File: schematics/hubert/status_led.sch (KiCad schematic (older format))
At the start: 8 parts, among them U8 ULN2003A

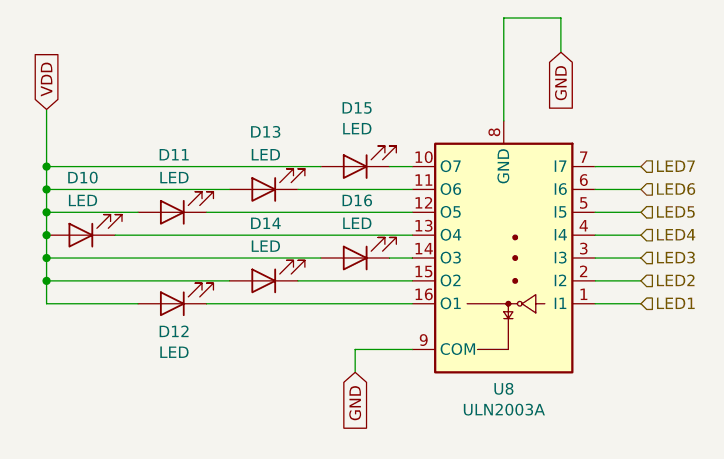
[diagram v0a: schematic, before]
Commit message: fixed ERC problems and added connector for input pins
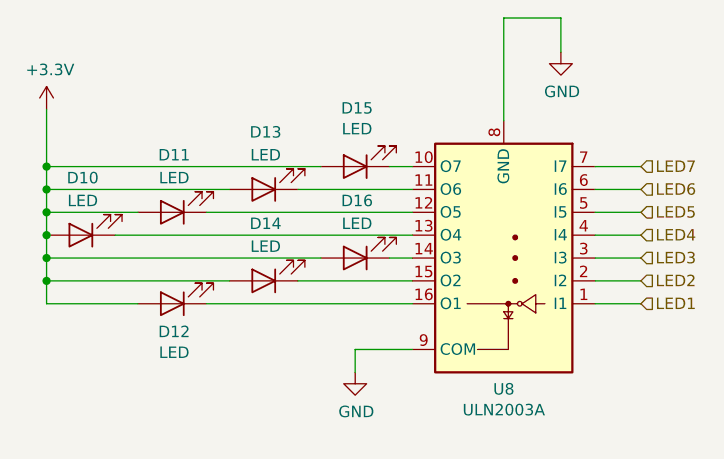
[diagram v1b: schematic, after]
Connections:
- net VDD renamed +3V3
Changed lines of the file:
@@
 Text HLabel 6850 3500 2    50   Input ~ 0
 LED7
-Text GLabel 5600 4400 3    50   Input ~ 0
-GND
 $Comp
 L Transistor_Array:ULN2003A U8
@@
 Wire Wire Line
 	5600 4300 5600 4400
-Text GLabel 6500 3000 3    50   Input ~ 0
-GND
 Wire Wire Line
 	6250 3300 6250 2850
@@
 Wire Wire Line
 	5450 3500 4250 3500
-Text GLabel 4250 3250 1    50   Input ~ 0
-VDD
 Wire Wire Line
 	4250 3250 4250 3500
@@
 Wire Wire Line
 	4250 4000 4250 4100
+$Comp
+L power:+3.3V #PWR0127
+U 1 1 5BE2D2EF
+P 4250 3250
+F 0 "#PWR0127" H 4250 3100 50  0001 C CNN
+F 1 "+3.3V" H 4265 3423 50  0000 C CNN
+F 2 "" H 4250 3250 50  0001 C CNN
+F 3 "" H 4250 3250 50  0001 C CNN
+	1    4250 3250
+	1    0    0    -1
+$EndComp
+$Comp
+L power:GND #PWR0128
+U 1 1 5BE2D328
+P 6500 3000
+F 0 "#PWR0128" H 6500 2750 50  0001 C CNN
+F 1 "GND" H 6505 2827 50  0000 C CNN
+F 2 "" H 6500 3000 50  0001 C CNN
+F 3 "" H 6500 3000 50  0001 C CNN
+	1    6500 3000
+	1    0    0    -1
+$EndComp
+$Comp
+L power:GND #PWR0129
+U 1 1 5BE2D361
+P 5600 4400
+F 0 "#PWR0129" H 5600 4150 50  0001 C CNN
+F 1 "GND" H 5605 4227 50  0000 C CNN
+F 2 "" H 5600 4400 50  0001 C CNN
+F 3 "" H 5600 4400 50  0001 C CNN
+	1    5600 4400
+	1    0    0    -1
+$EndComp
 $EndSCHEMATC

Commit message: started working on layout
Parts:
- D10, D11, D12, D13, D14, D15, D16: footprint (none) -> LED_THT:LED_D5.0mm
- U8: footprint (none) -> Package_DIP:DIP-16_W7.62mm_Socket
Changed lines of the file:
@@
 Sheet 7 7
 Title "Hubert"
-Date "2018-11-02"
-Rev "1.1"
+Date "2018-11-05"
+Rev "1.2"
 Comp ""
 Comment1 ""
@@
 F 0 "U8" H 6250 4474 50  0000 C CNN
 F 1 "ULN2003A" H 6250 4565 50  0000 C CNN
-F 2 "" H 6300 3350 50  0001 L CNN
+F 2 "Package_DIP:DIP-16_W7.62mm_Socket" H 6300 3350 50  0001 L CNN
 F 3 "http://www.ti.com/lit/ds/symlink/uln2003a.pdf" H 6350 3700 50  0001 C CNN
 	1    6250 3900
@@
 F 0 "D15" H 5592 3245 50  0000 C CNN
 F 1 "LED" H 5592 3336 50  0000 C CNN
-F 2 "" H 5600 3500 50  0001 C CNN
+F 2 "LED_THT:LED_D5.0mm" H 5600 3500 50  0001 C CNN
 F 3 "~" H 5600 3500 50  0001 C CNN
 	1    5600 3500
@@
 F 0 "D13" H 5192 3350 50  0000 C CNN
 F 1 "LED" H 5192 3450 50  0000 C CNN
-F 2 "" H 5200 3600 50  0001 C CNN
+F 2 "LED_THT:LED_D5.0mm" H 5200 3600 50  0001 C CNN
 F 3 "~" H 5200 3600 50  0001 C CNN
 	1    5200 3600
@@
 F 0 "D11" H 4792 3450 50  0000 C CNN
 F 1 "LED" H 4792 3550 50  0000 C CNN
-F 2 "" H 4800 3700 50  0001 C CNN
+F 2 "LED_THT:LED_D5.0mm" H 4800 3700 50  0001 C CNN
 F 3 "~" H 4800 3700 50  0001 C CNN
 	1    4800 3700
@@
 F 0 "D10" H 4392 3550 50  0000 C CNN
 F 1 "LED" H 4392 3650 50  0000 C CNN
-F 2 "" H 4400 3800 50  0001 C CNN
+F 2 "LED_THT:LED_D5.0mm" H 4400 3800 50  0001 C CNN
 F 3 "~" H 4400 3800 50  0001 C CNN
 	1    4400 3800
@@
 F 0 "D16" H 5592 3650 50  0000 C CNN
 F 1 "LED" H 5592 3750 50  0000 C CNN
-F 2 "" H 5600 3900 50  0001 C CNN
+F 2 "LED_THT:LED_D5.0mm" H 5600 3900 50  0001 C CNN
 F 3 "~" H 5600 3900 50  0001 C CNN
 	1    5600 3900
@@
 F 0 "D14" H 5192 3750 50  0000 C CNN
 F 1 "LED" H 5192 3850 50  0000 C CNN
-F 2 "" H 5200 4000 50  0001 C CNN
+F 2 "LED_THT:LED_D5.0mm" H 5200 4000 50  0001 C CNN
 F 3 "~" H 5200 4000 50  0001 C CNN
 	1    5200 4000
@@
 F 0 "D12" H 4792 4223 50  0000 C CNN
 F 1 "LED" H 4792 4314 50  0000 C CNN
-F 2 "" H 4800 4100 50  0001 C CNN
+F 2 "LED_THT:LED_D5.0mm" H 4800 4100 50  0001 C CNN
 F 3 "~" H 4800 4100 50  0001 C CNN
 	1    4800 4100
